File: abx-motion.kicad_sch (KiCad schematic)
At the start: 0 parts

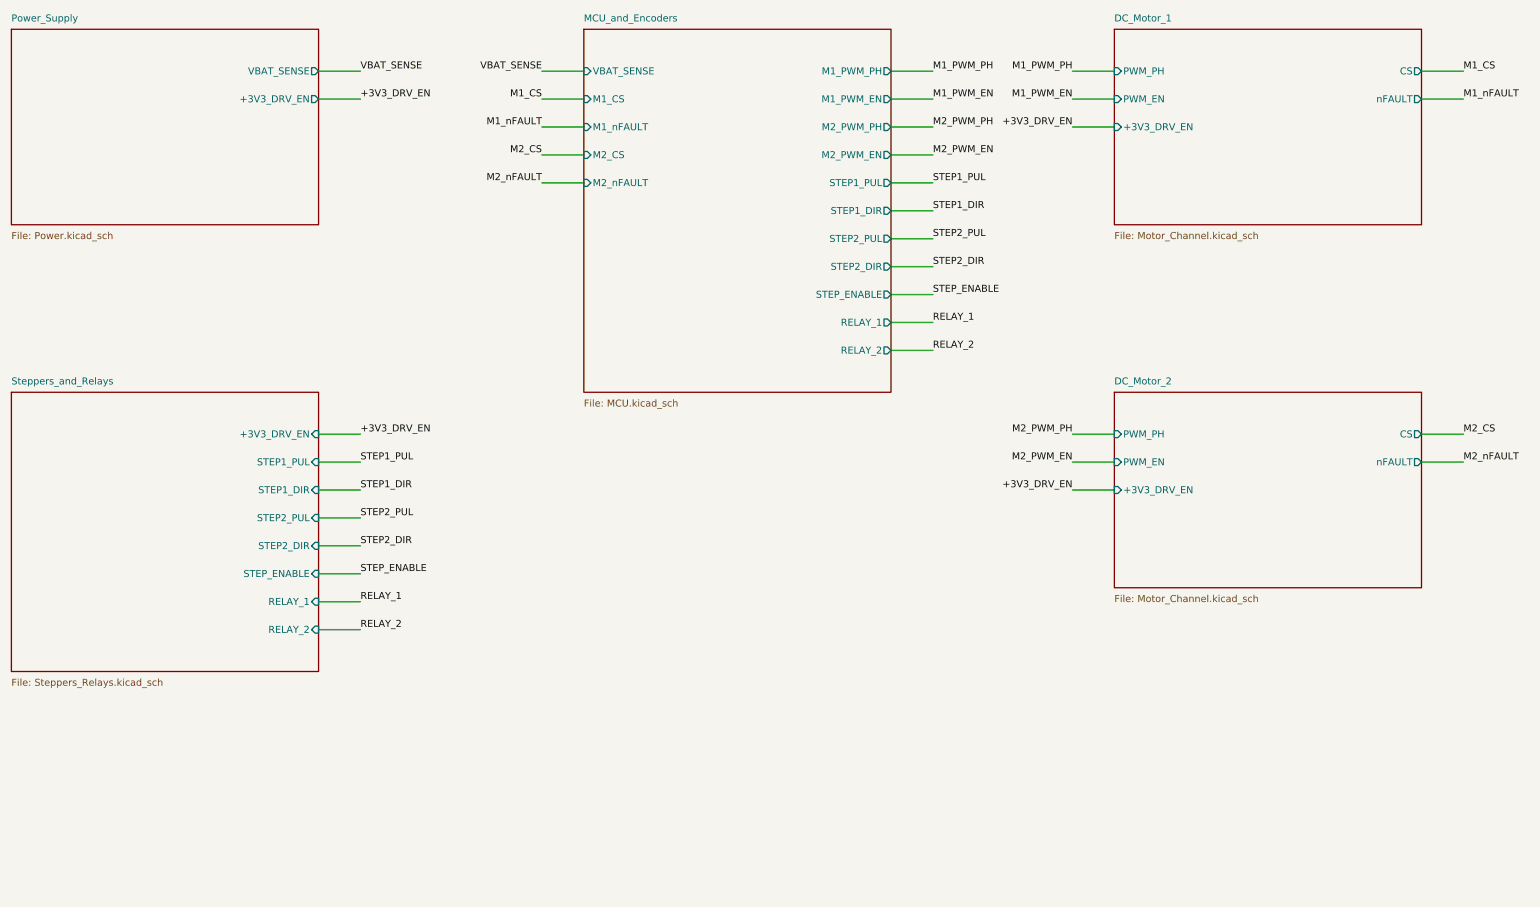
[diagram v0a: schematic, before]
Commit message: Complete V1.1 compact 6-channel I/O & DC output architecture (0 ERC, 0 DRC errors, 0 unconnected, 0 parity)
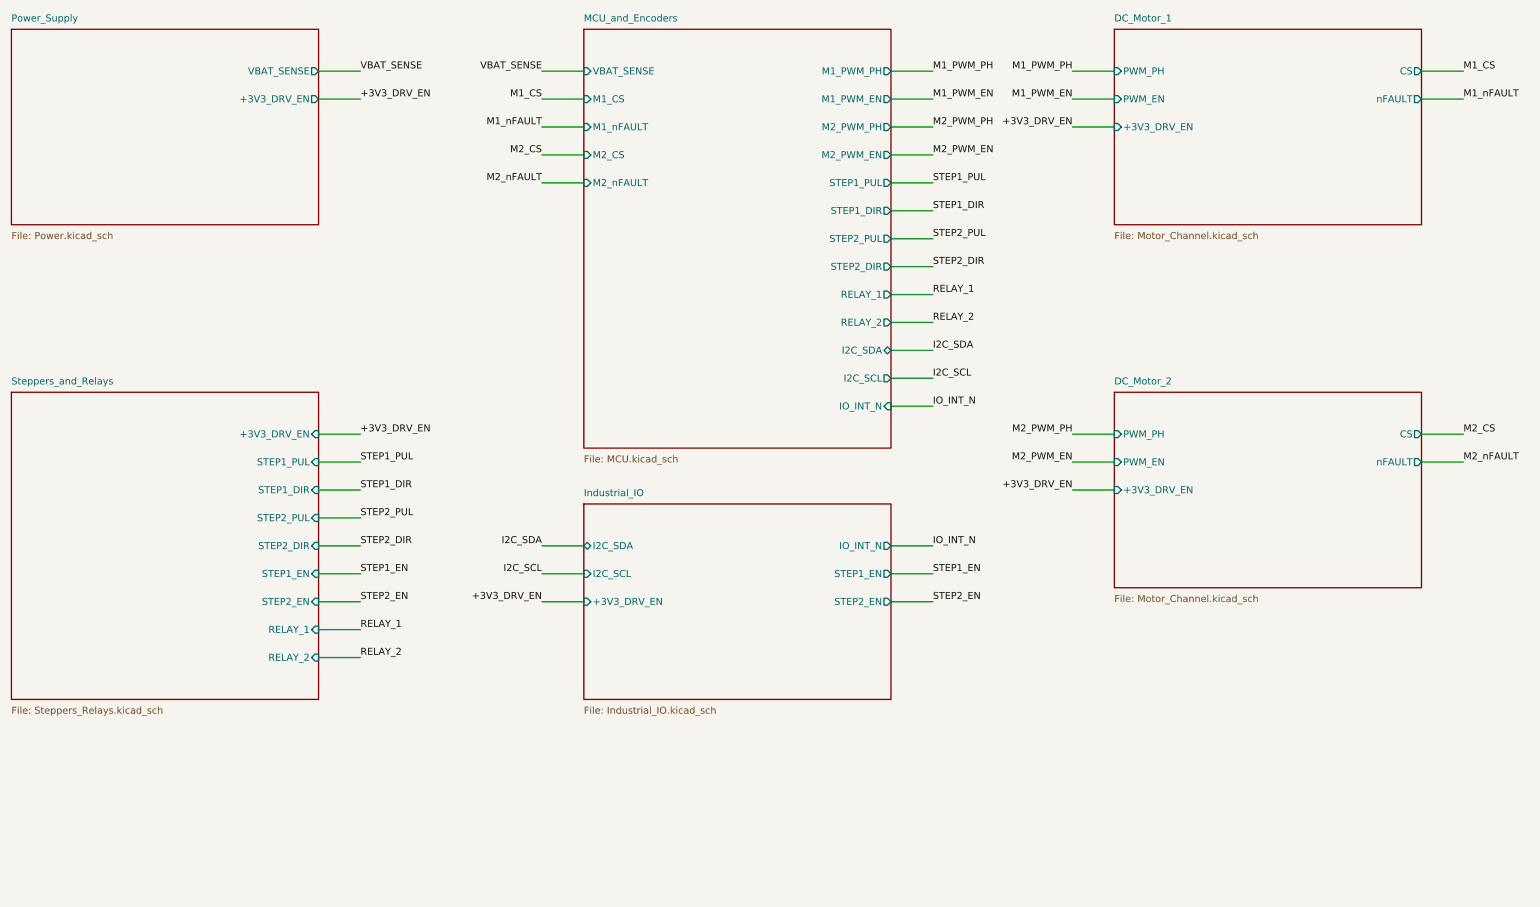
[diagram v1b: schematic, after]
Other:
- added sheet Industrial_IO (Industrial_IO.kicad_sch)
- sheet MCU_and_Encoders ports: added I2C_SCL, I2C_SDA, IO_INT_N; removed STEP_ENABLE
- sheet Steppers_and_Relays ports: added STEP1_EN, STEP2_EN; removed STEP_ENABLE
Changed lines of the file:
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@@
 	(wire (pts (xy 180.34 83.82) (xy 187.96 83.82)) (stroke (width 0) (type default)))
 	(wire (pts (xy 180.34 88.9) (xy 187.96 88.9)) (stroke (width 0) (type default)))
+	(wire (pts (xy 180.34 93.98) (xy 187.96 93.98)) (stroke (width 0) (type default)))
+	(wire (pts (xy 180.34 99.06) (xy 187.96 99.06)) (stroke (width 0) (type default)))
 	(wire (pts (xy 220.98 38.1) (xy 213.36 38.1)) (stroke (width 0) (type default)))
 	(wire (pts (xy 220.98 43.18) (xy 213.36 43.18)) (stroke (width 0) (type default)))
@@
 	(wire (pts (xy 76.2 134.62) (xy 83.82 134.62)) (stroke (width 0) (type default)))
 	(wire (pts (xy 76.2 139.7) (xy 83.82 139.7)) (stroke (width 0) (type default)))
+	(wire (pts (xy 76.2 144.78) (xy 83.82 144.78)) (stroke (width 0) (type default)))
+	(wire (pts (xy 124.46 124.46) (xy 116.84 124.46)) (stroke (width 0) (type default)))
+	(wire (pts (xy 124.46 129.54) (xy 116.84 129.54)) (stroke (width 0) (type default)))
+	(wire (pts (xy 124.46 134.62) (xy 116.84 134.62)) (stroke (width 0) (type default)))
+	(wire (pts (xy 180.34 124.46) (xy 187.96 124.46)) (stroke (width 0) (type default)))
+	(wire (pts (xy 180.34 129.54) (xy 187.96 129.54)) (stroke (width 0) (type default)))
+	(wire (pts (xy 180.34 134.62) (xy 187.96 134.62)) (stroke (width 0) (type default)))
 	(label "VBAT_SENSE" (at 83.82 38.1 0) (fields_autoplaced yes) (effects (font (size 1.27 1.27)) (justify left bottom)))
 	(label "+3V3_DRV_EN" (at 83.82 43.18 0) (fields_autoplaced yes) (effects (font (size 1.27 1.27)) (justify left bottom)))
@@
 	(label "STEP2_PUL" (at 187.96 68.58 0) (fields_autoplaced yes) (effects (font (size 1.27 1.27)) (justify left bottom)))
 	(label "STEP2_DIR" (at 187.96 73.66 0) (fields_autoplaced yes) (effects (font (size 1.27 1.27)) (justify left bottom)))
-	(label "STEP_ENABLE" (at 187.96 78.74 0) (fields_autoplaced yes) (effects (font (size 1.27 1.27)) (justify left bottom)))
-	(label "RELAY_1" (at 187.96 83.82 0) (fields_autoplaced yes) (effects (font (size 1.27 1.27)) (justify left bottom)))
-	(label "RELAY_2" (at 187.96 88.9 0) (fields_autoplaced yes) (effects (font (size 1.27 1.27)) (justify left bottom)))
+	(label "RELAY_1" (at 187.96 78.74 0) (fields_autoplaced yes) (effects (font (size 1.27 1.27)) (justify left bottom)))
+	(label "RELAY_2" (at 187.96 83.82 0) (fields_autoplaced yes) (effects (font (size 1.27 1.27)) (justify left bottom)))
+	(label "I2C_SDA" (at 187.96 88.9 0) (fields_autoplaced yes) (effects (font (size 1.27 1.27)) (justify left bottom)))
+	(label "I2C_SCL" (at 187.96 93.98 0) (fields_autoplaced yes) (effects (font (size 1.27 1.27)) (justify left bottom)))
+	(label "IO_INT_N" (at 187.96 99.06 0) (fields_autoplaced yes) (effects (font (size 1.27 1.27)) (justify left bottom)))
 	(label "M1_PWM_PH" (at 213.36 38.1 180) (fields_autoplaced yes) (effects (font (size 1.27 1.27)) (justify right bottom)))
 	(label "M1_PWM_EN" (at 213.36 43.18 180) (fields_autoplaced yes) (effects (font (size 1.27 1.27)) (justify right bottom)))
@@
 	(label "STEP2_PUL" (at 83.82 119.38 0) (fields_autoplaced yes) (effects (font (size 1.27 1.27)) (justify left bottom)))
 	(label "STEP2_DIR" (at 83.82 124.46 0) (fields_autoplaced yes) (effects (font (size 1.27 1.27)) (justify left bottom)))
-	(label "STEP_ENABLE" (at 83.82 129.54 0) (fields_autoplaced yes) (effects (font (size 1.27 1.27)) (justify left bottom)))
-	(label "RELAY_1" (at 83.82 134.62 0) (fields_autoplaced yes) (effects (font (size 1.27 1.27)) (justify left bottom)))
-	(label "RELAY_2" (at 83.82 139.7 0) (fields_autoplaced yes) (effects (font (size 1.27 1.27)) (justify left bottom)))
+	(label "STEP1_EN" (at 83.82 129.54 0) (fields_autoplaced yes) (effects (font (size 1.27 1.27)) (justify left bottom)))
+	(label "STEP2_EN" (at 83.82 134.62 0) (fields_autoplaced yes) (effects (font (size 1.27 1.27)) (justify left bottom)))
+	(label "RELAY_1" (at 83.82 139.7 0) (fields_autoplaced yes) (effects (font (size 1.27 1.27)) (justify left bottom)))
+	(label "RELAY_2" (at 83.82 144.78 0) (fields_autoplaced yes) (effects (font (size 1.27 1.27)) (justify left bottom)))
+	(label "I2C_SDA" (at 116.84 124.46 180) (fields_autoplaced yes) (effects (font (size 1.27 1.27)) (justify right bottom)))
+	(label "I2C_SCL" (at 116.84 129.54 180) (fields_autoplaced yes) (effects (font (size 1.27 1.27)) (justify right bottom)))
+	(label "+3V3_DRV_EN" (at 116.84 134.62 180) (fields_autoplaced yes) (effects (font (size 1.27 1.27)) (justify right bottom)))
+	(label "IO_INT_N" (at 187.96 124.46 0) (fields_autoplaced yes) (effects (font (size 1.27 1.27)) (justify left bottom)))
+	(label "STEP1_EN" (at 187.96 129.54 0) (fields_autoplaced yes) (effects (font (size 1.27 1.27)) (justify left bottom)))
+	(label "STEP2_EN" (at 187.96 134.62 0) (fields_autoplaced yes) (effects (font (size 1.27 1.27)) (justify left bottom)))
 	(sheet
 		(at 20.32 30.48)
@@
 	(sheet
 		(at 124.46 30.48)
-		(size 55.88 66.04)
+		(size 55.88 76.2)
 		(fields_autoplaced yes)
 		(stroke
@@
 		)
 		(property "Sheetfile" "MCU.kicad_sch"
-			(at 124.46 97.79 0)
+			(at 124.46 107.95 0)
 			(effects
 				(font
@@
 			)
 		)
-		(pin "STEP_ENABLE" output
+		(pin "RELAY_1" output
 			(at 180.34 78.74 0)
 			(effects
@@
 			)
 		)
-		(pin "RELAY_1" output
+		(pin "RELAY_2" output
 			(at 180.34 83.82 0)
 			(effects
@@
 			)
 		)
-		(pin "RELAY_2" output
+		(pin "I2C_SDA" bidirectional
 			(at 180.34 88.9 0)
+			(effects
+				(font
+					(size 1.27 1.27)
+				)
+				(justify right)
+			)
+		)
+		(pin "I2C_SCL" output
+			(at 180.34 93.98 0)
+			(effects
+				(font
+					(size 1.27 1.27)
+				)
+				(justify right)
+			)
+		)
+		(pin "IO_INT_N" input
+			(at 180.34 99.06 0)
 			(effects
 				(font
@@
 	(sheet
 		(at 20.32 96.52)
-		(size 55.88 50.8)
+		(size 55.88 55.88)
 		(fields_autoplaced yes)
 		(stroke
@@
 		)
 		(property "Sheetfile" "Steppers_Relays.kicad_sch"
-			(at 20.32 148.59 0)
+			(at 20.32 153.67 0)
 			(effects
 				(font
@@
 			)
 		)
-		(pin "STEP_ENABLE" input
+		(pin "STEP1_EN" input
 			(at 76.2 129.54 0)
 			(effects
@@
 			)
 		)
+		(pin "STEP2_EN" input
+			(at 76.2 134.62 0)
+			(effects
+				(font
+					(size 1.27 1.27)
+				)
+				(justify right)
+			)
+		)
 		(pin "RELAY_1" input
-			(at 76.2 134.62 0)
+			(at 76.2 139.7 0)
 			(effects
 				(font
@@
 		)
 		(pin "RELAY_2" input
-			(at 76.2 139.7 0)
+			(at 76.2 144.78 0)
 			(effects
 				(font
@@
 		)
 	)
+	(sheet
+		(at 124.46 116.84)
+		(size 55.88 35.56)
+		(fields_autoplaced yes)
+		(stroke
+			(width 0.1524)
+			(type solid)
+		)
+		(fill
+			(color 0 0 0 0.0000)
+		)
+		(property "Sheetname" "Industrial_IO"
+			(at 124.46 115.57 0)
+			(effects
+				(font
+					(size 1.27 1.27)
+				)
+				(justify left bottom)
+			)
+		)
+		(property "Sheetfile" "Industrial_IO.kicad_sch"
+			(at 124.46 153.67 0)
+			(effects
+				(font
+					(size 1.27 1.27)
+				)
+				(justify left top)
+			)
+		)
+		(pin "I2C_SDA" bidirectional
+			(at 124.46 124.46 180)
+			(effects
+				(font
+					(size 1.27 1.27)
+				)
+				(justify left)
+			)
+		)
+		(pin "I2C_SCL" input
+			(at 124.46 129.54 180)
+			(effects
+				(font
+					(size 1.27 1.27)
+				)
+				(justify left)
+			)
+		)
+		(pin "+3V3_DRV_EN" input
+			(at 124.46 134.62 180)
+			(effects
+				(font
+					(size 1.27 1.27)
+				)
+				(justify left)
+			)
+		)
+		(pin "IO_INT_N" output
+			(at 180.34 124.46 0)
+			(effects
+				(font
+					(size 1.27 1.27)
+				)
+				(justify right)
+			)
+		)
+		(pin "STEP1_EN" output
+			(at 180.34 129.54 0)
+			(effects
+				(font
+					(size 1.27 1.27)
+				)
+				(justify right)
+			)
+		)
+		(pin "STEP2_EN" output
+			(at 180.34 134.62 0)
+			(effects
+				(font
+					(size 1.27 1.27)
+				)
+				(justify right)
+			)
+		)
+		(instances
+			(project "abx-motion"
+				(path "/f9149098-3f23-438d-bdc2-2e278b5ca35b"
+					(page "7")
+				)
+			)
+		)
+	)
 	(sheet_instances
 		(path "/"
@@
 			(page "6")
 		)
+		(path "/f9149098-3f23-438d-bdc2-2e278b5ca35b/5b34e428-8262-458c-b688-d5bdfede8a4e"
+			(page "7")
+		)
 	)

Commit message: Finalize Rev 1.1d robustness, thermal layout and manufacturing package
Preserve sensing and current-limit fixes, assembly part/rotation corrections,
D2 package changes, revision markings and incremental thermal copper/vias.
Archive the working checkpoints and supplier/validation evidence alongside
matched Gerbers, BOM, CPL, schematic PDF, renders and hash manifests.

Current Rev 1.1d: ERC 0; DRC 0 errors, 0 opens and 0 parity issues,
with 19 existing library footprint warnings. Preserve original routing and
component placements; physical powered qualification is not yet performed.
Relay alignment requires assembler review before assembly.
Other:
- title: (none) -> ABX-Motion
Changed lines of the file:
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@@
 	(generator_version "10.0")
 	(paper "A4")
+	(title_block (title "ABX-Motion") (rev "1.1d"))
 	(wire (pts (xy 76.2 38.1) (xy 83.82 38.1)) (stroke (width 0) (type default)))
 	(wire (pts (xy 76.2 43.18) (xy 83.82 43.18)) (stroke (width 0) (type default)))

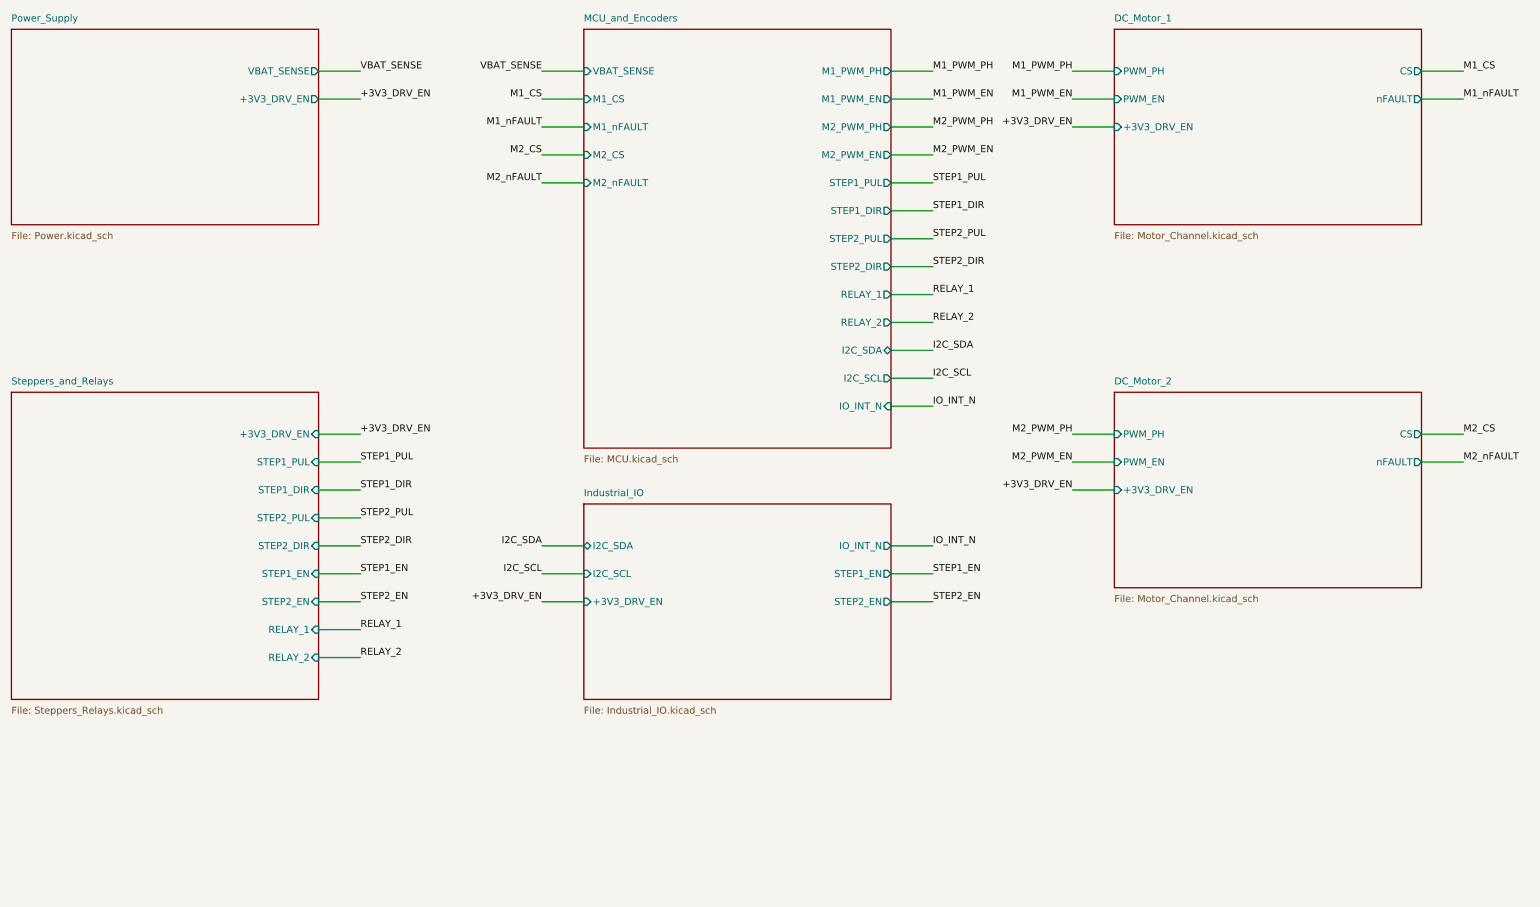
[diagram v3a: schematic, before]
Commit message: Save Rev 1.2a three-axis checkpoint and audited JLCPCB exports
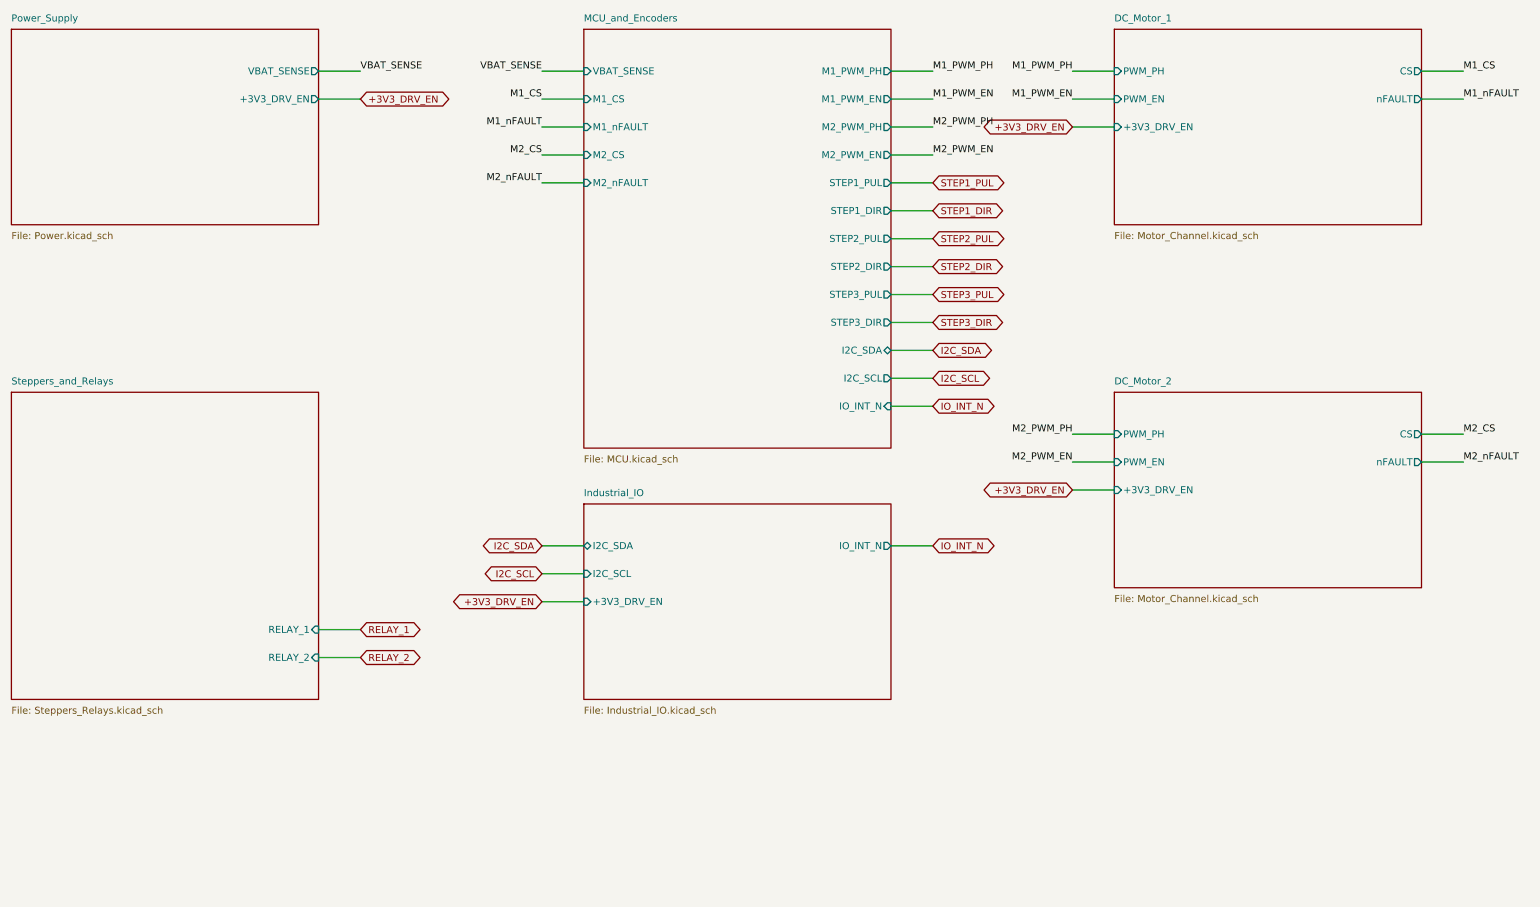
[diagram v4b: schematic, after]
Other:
- sheet Industrial_IO ports: added none; removed STEP1_EN, STEP2_EN
- sheet MCU_and_Encoders ports: added STEP3_DIR, STEP3_PUL; removed RELAY_1, RELAY_2
- sheet Steppers_and_Relays ports: added none; removed +3V3_DRV_EN, STEP1_DIR, STEP1_EN, STEP1_PUL, STEP2_DIR, STEP2_EN, STEP2_PUL

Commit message: Promote reviewed Ethernet draft into root abx-motion project
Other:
- added sheet Ethernet_Power (Ethernet_Power.kicad_sch)
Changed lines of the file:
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@@
 	(title_block
 		(title "ABX-Motion")
-		(rev "1.2a")
+		(rev "1.2b INTEGRATION DRAFT")
 	)
 	(wire
@@
 	)
 	(embedded_fonts no)
+	(sheet
+		(at 220.98 165.1)
+		(size 66.04 20.32)
+		(stroke
+			(width 0)
+			(type default)
+		)
+		(fill
+			(color 0 0 0 0)
+		)
+		(property "Sheetname" "Ethernet_Power"
+			(at 220.98 164.49 0)
+			(effects
+				(font
+					(size 1.27 1.27)
+				)
+				(justify left bottom)
+			)
+		)
+		(property "Sheetfile" "Ethernet_Power.kicad_sch"
+			(at 220.98 186.03 0)
+			(effects
+				(font
+					(size 1.27 1.27)
+				)
+				(justify left top)
+			)
+		)
+		(instances
+			(project "abx-motion"
+				(path "/f9149098-3f23-438d-bdc2-2e278b5ca35b"
+					(page "8")
+				)
+			)
+		)
+	)
 )
